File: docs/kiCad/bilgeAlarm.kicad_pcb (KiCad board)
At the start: 2 copper layers, 111.8 x 88.9 mm, 67 parts, among them J1 PUMP IN, J10 LCD_SDA, J11 LCD_SCL, J12 LCD_GND, J13 ALARM+, J14 ALARM-, J15 LED_GND, J16 LED_GND, J17 LED_DATA, J18 LED_DATA, J19 LED_5V, J2 PUMP2 IN, J20 LED_5V, J21 AUX, J22 AUX, J23 AUX, J24 AUX, J25 AUX, J26 AUX, J27 AUX, J28 AUX, J29 AUX, J3 PUMP OUT, J30 AUX, J31 AUX, J32 AUX, J33 AUX, J34 AUX, J35 AUX, J36 AUX, J37 AUX, J38 AUX, J39 AUX, J4 12V, J40 AUX, J41 AUX, J5 GND, J6 LED_5V, J7 LED_DATA, J8 LED_GND, J9 LCD_5V, K1 RELAY, M1 BUCK01, M2 SD_TYP0, Q1 IRLZ44N, Q2 BCS547, SW1 POWER, SW2 BUTTON1, SW3 BUTTON2, SW4 BUTTON3, U1 ESP32_DEV_0

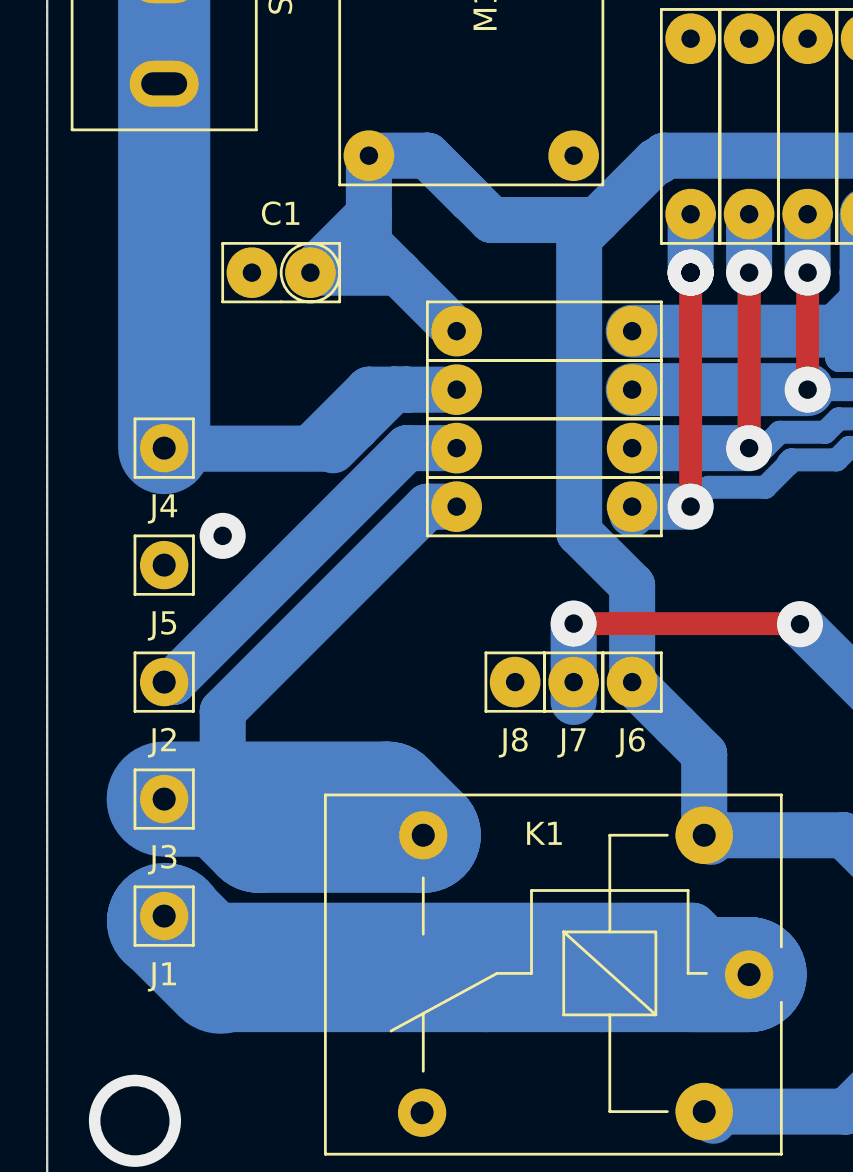
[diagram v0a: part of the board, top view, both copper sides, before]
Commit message: reworked bilgeAlarm gcode
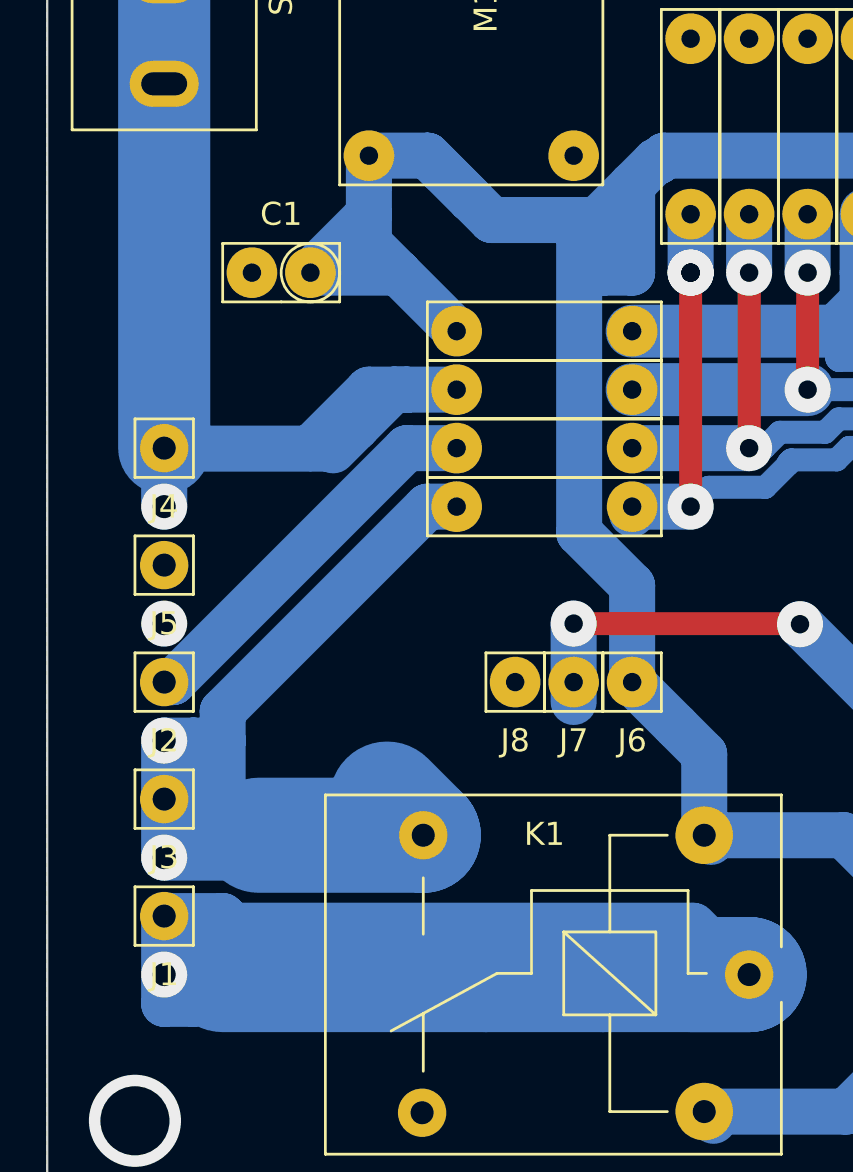
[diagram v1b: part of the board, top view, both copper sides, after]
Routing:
- net PUMP_OUT: track 39.6 -> 52.4 mm, vias 0 -> 2
- net PUMP_IN: track 58.8 -> 65.3 mm, vias 0 -> 1
- net +5V: track 168.4 -> 174.8 mm
- net RAW_12V: track 38.4 -> 40.9 mm, vias 0 -> 1
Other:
- board text added: "January 2022"
- board text removed: "December 2021"
